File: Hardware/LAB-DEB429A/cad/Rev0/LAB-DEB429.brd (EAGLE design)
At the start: 149.9 x 120.7 mm, 102 parts, among them J1 TSW-132-02-S-D, J2 TSW-132-02-S-D, U1 LAB-ADSM300F, U10 SF-MICROSD, U11 25MPX, U12 LAB-PPS330D, U13 LAB-PPS330D, U14 LAB-PPS330D, U15 SI1143, U16 LAB-PPS330D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

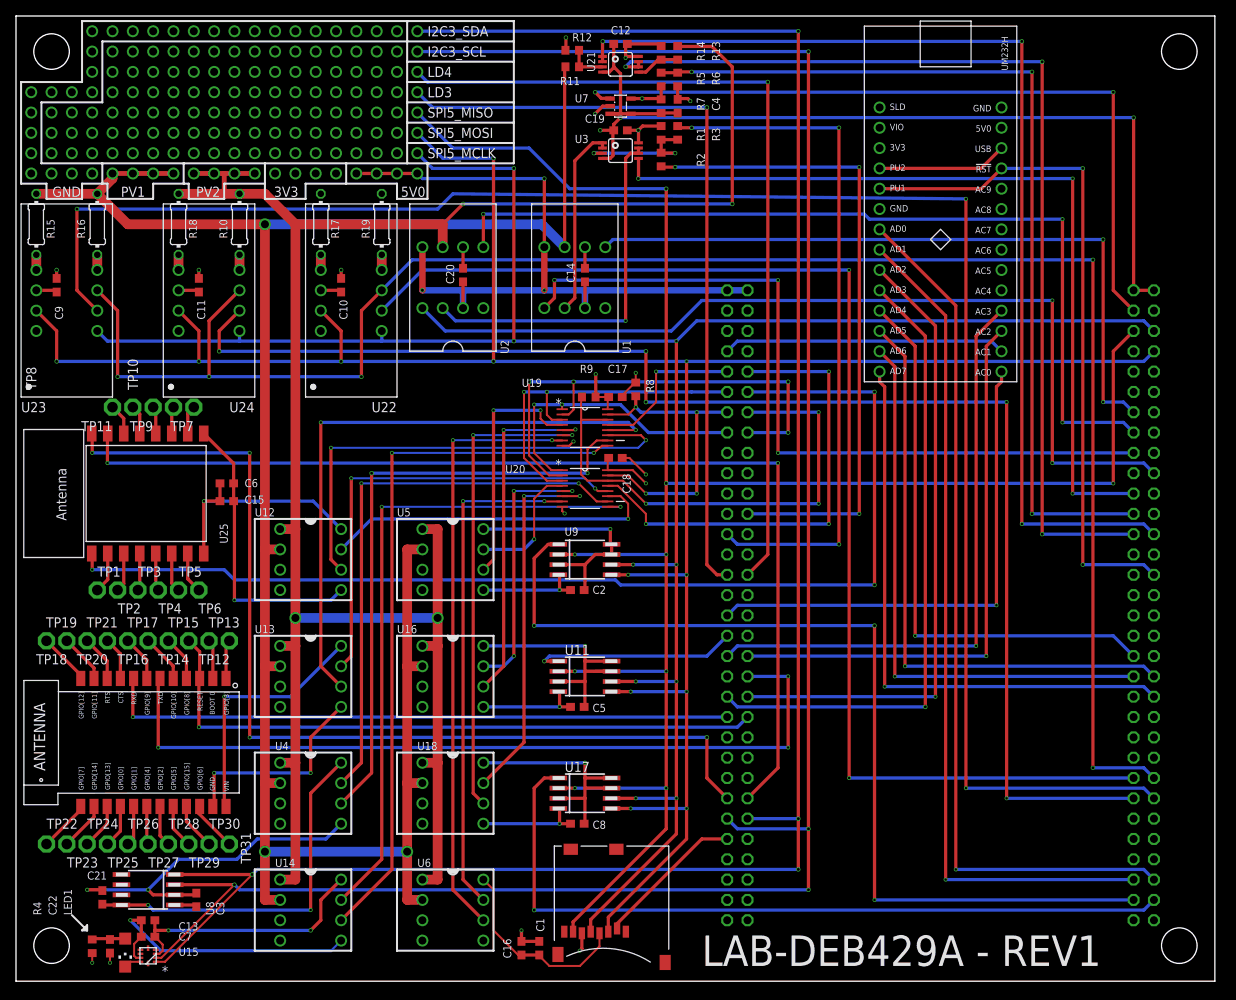
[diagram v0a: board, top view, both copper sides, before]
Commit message: 1) Updating the BOMs to synchronize purchasing.
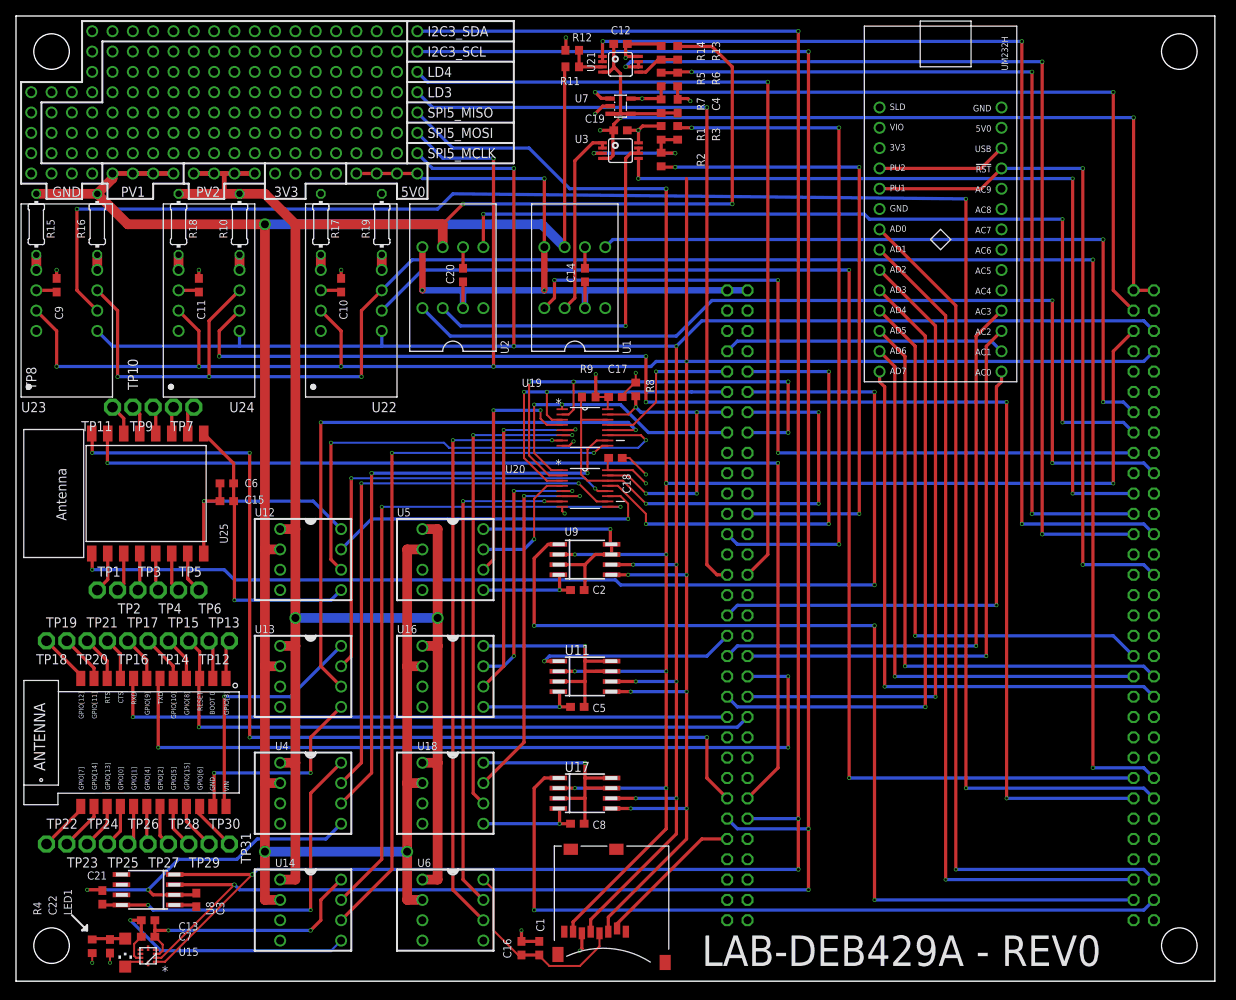
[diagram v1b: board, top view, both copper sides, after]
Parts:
- C22: value 10u -> 47u
- R1: value 51K -> (none)
- R11, R12, R13, R14, R8, R9: value 100K -> (none)
- R2: value 39K -> (none)
- R3: value 18.4K -> (none)
- R7: value 0R1 -> 0.13R
- U7: value MAX4376HAUK -> MAX4376
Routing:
- net SPI5_MOSI: track 299.6 -> 325.2 mm
- net SPI5_MCLK: track 273.7 -> 275.5 mm
- net WF_VSEL0: track 60.6 -> 61.5 mm
- net VADJ2: track 46.4 -> 47.3 mm
- net ADC1_PII2: track 115.0 -> 115.6 mm
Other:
- board text added: "LAB-DEB429A - REV0"
- board text removed: "LAB-DEB429A - REV1"
